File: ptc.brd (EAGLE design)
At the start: 40.6 x 48.3 mm, 6 parts

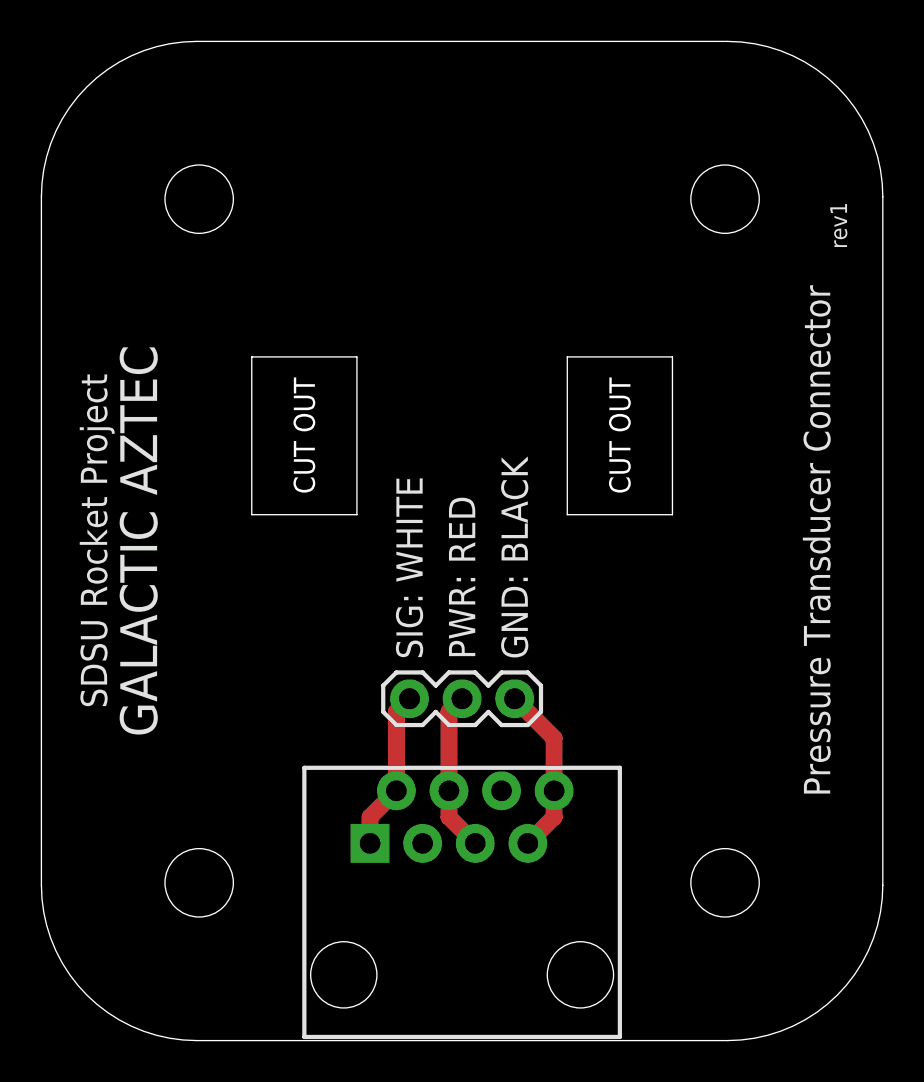
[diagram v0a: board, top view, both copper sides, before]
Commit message: Replaced thru holes with custom Eagle component that had larger thru holes. Adjusted cut out section. Added PCB images rendered by OSHPark. Added README.md.
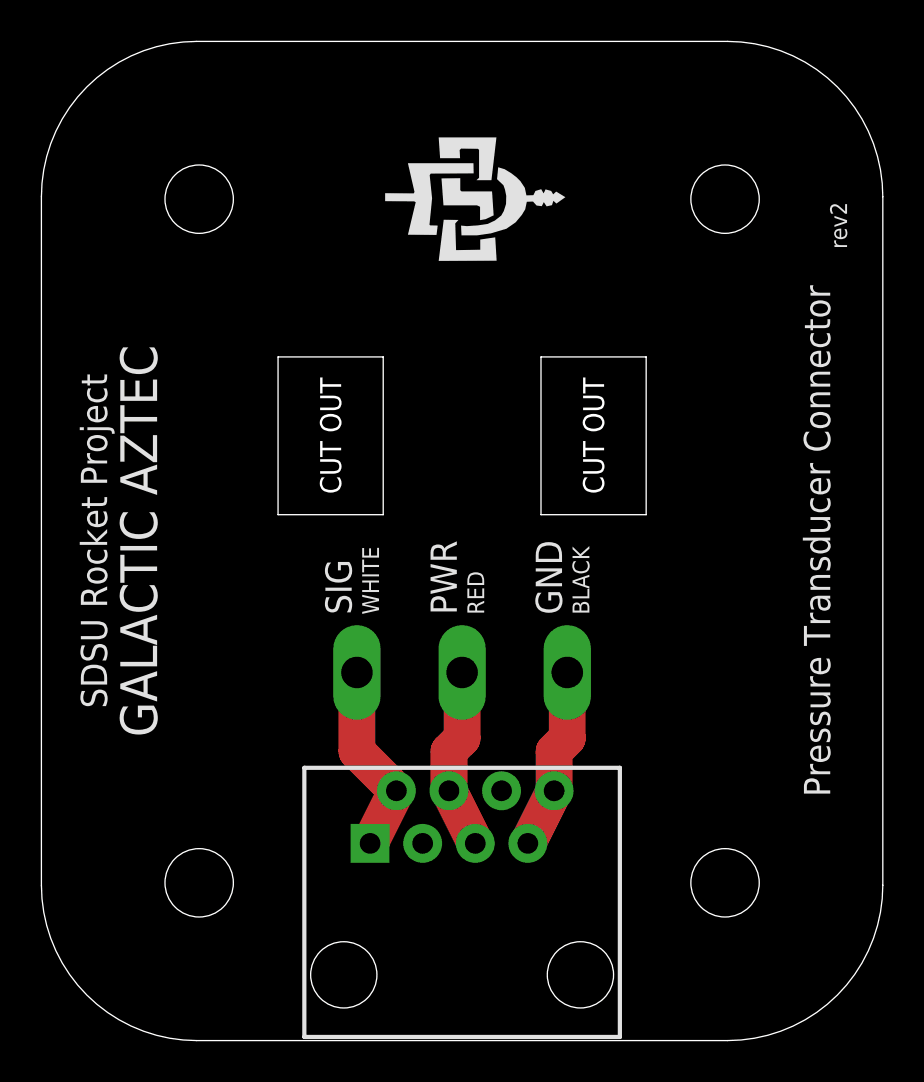
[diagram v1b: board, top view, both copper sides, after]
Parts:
- JP2: value (none) -> PRESS-TRANS-3POS; device SparkFun-Connectors:1X03 -> SDSURocket-Connectors:PRESSURE-TRANSDUCER-3POS
- moved JP2 2.84 mm to (20.3, 17.8)
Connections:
- net GND renamed N$3
- net PWR renamed N$2
- net SIG renamed N$1
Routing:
- net N$1: track 7.77 -> 9.34 mm
- net N$2: track 7.77 -> 8.82 mm
- net N$3: track 8.30 -> 8.82 mm
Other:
- outline, holes or cut-outs redrawn
- board text added: "rev2"
- board text removed: "GND: BLACK"
- board text removed: "PWR: RED"
- board text removed: "SIG: WHITE"
- board text removed: "rev1"
